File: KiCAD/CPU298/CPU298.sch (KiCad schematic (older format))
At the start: 1 part

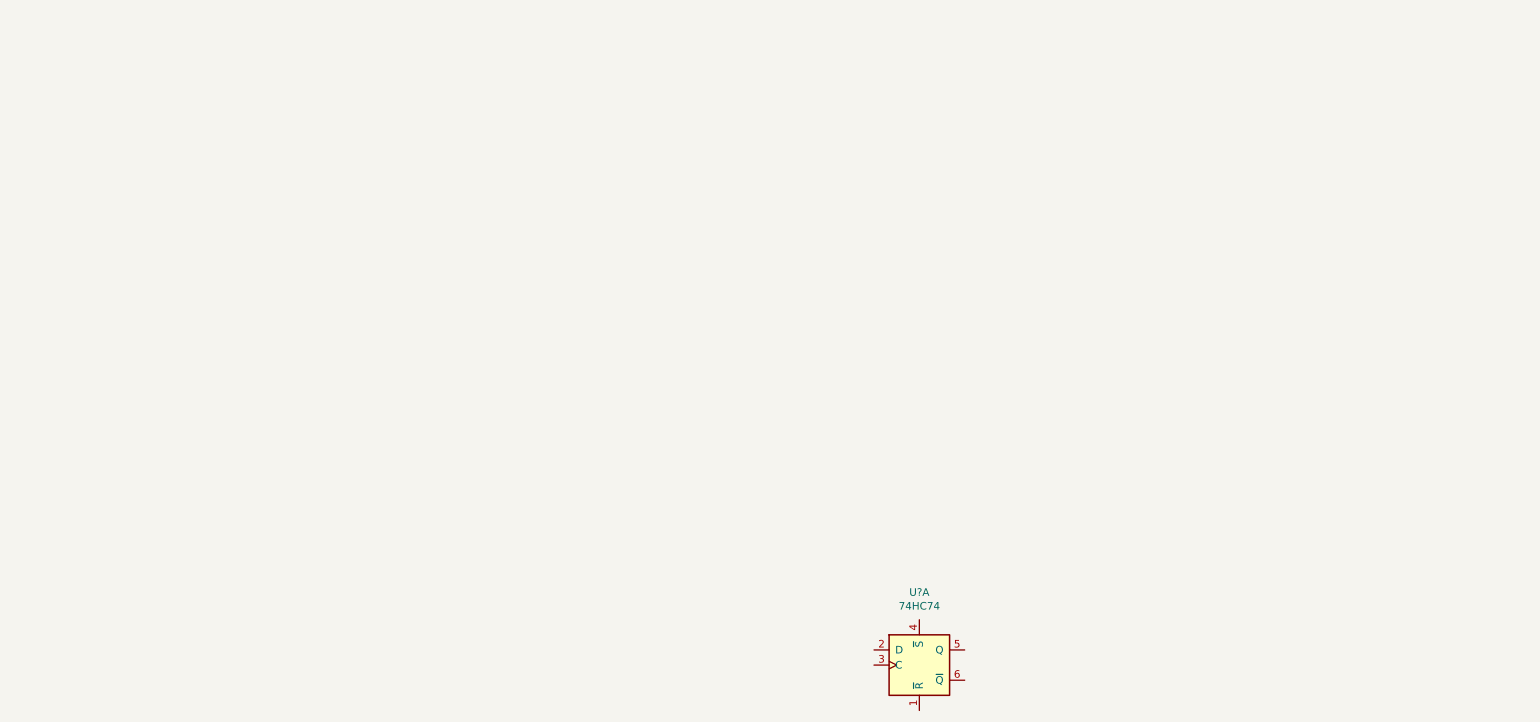
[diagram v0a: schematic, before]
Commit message: 8bit offset adder.
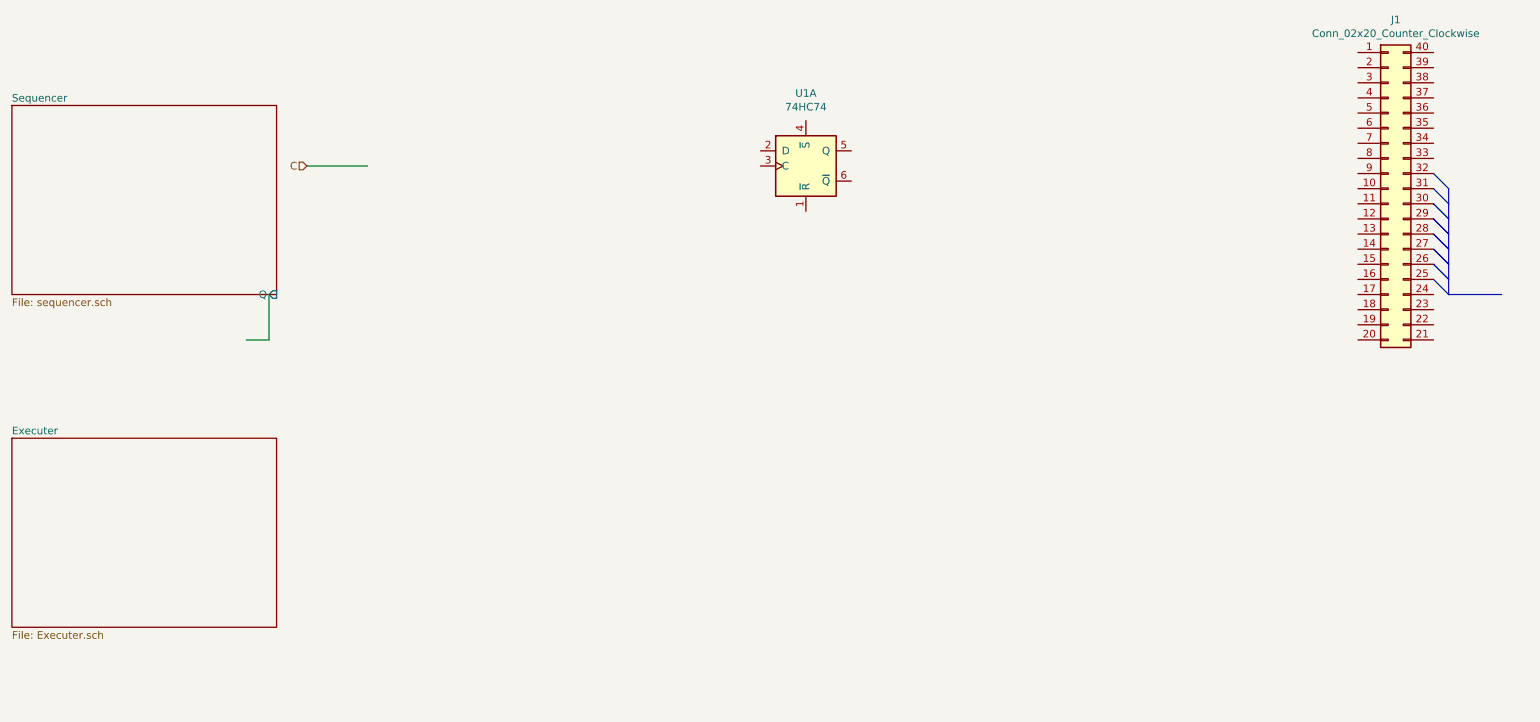
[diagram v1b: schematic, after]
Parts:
- added J1: Conn_02x20_Counter_Clockwise, symbol Connector_Generic:Conn_02x20_Counter_Clockwise
- gave numbers to parts that had none: 1
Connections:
- net labels added: C
- wire segments 0 -> 3
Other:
- moved on the sheet: U1A
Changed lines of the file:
@@
 $Descr A4 11693 8268
 encoding utf-8
-Sheet 1 1
+Sheet 1 3
 Title ""
 Date ""
@@
 $EndDescr
 $Comp
-L 74xx:74HC74 U?
+L 74xx:74HC74 U1
 U 1 1 61108220
-P 7050 5500
-F 0 "U?" H 7050 5981 50  0000 C CNN
-F 1 "74HC74" H 7050 5890 50  0000 C CNN
-F 2 "" H 7050 5500 50  0001 C CNN
-F 3 "74xx/74hc_hct74.pdf" H 7050 5500 50  0001 C CNN
-	1    7050 5500
+P 6300 2200
+F 0 "U1" H 6300 2681 50  0000 C CNN
+F 1 "74HC74" H 6300 2590 50  0000 C CNN
+F 2 "" H 6300 2200 50  0001 C CNN
+F 3 "74xx/74hc_hct74.pdf" H 6300 2200 50  0001 C CNN
+	1    6300 2200
 	1    0    0    -1
 $EndComp
+$Sheet
+S 1050 1800 1750 1250
+U 64746FA5
+F0 "Sequencer" 50
+F1 "sequencer.sch" 50
+F2 "Q" I R 2800 3050 50
+$EndSheet
+$Sheet
+S 1050 4000 1750 1250
+U 6474704B
+F0 "Executer" 50
+F1 "Executer.sch" 50
+$EndSheet
+$Comp
+L Connector_Generic:Conn_02x20_Counter_Clockwise J1
+U 1 1 6474722C
+P 10150 2350
+F 0 "J1" H 10200 3467 50  0000 C CNN
+F 1 "Conn_02x20_Counter_Clockwise" H 10200 3376 50  0000 C CNN
+F 2 "" H 10150 2350 50  0001 C CNN
+F 3 "~" H 10150 2350 50  0001 C CNN
+	1    10150 2350
+	1    0    0    -1
+$EndComp
+Entry Bus Bus
+	10450 2250 10550 2350
+Entry Bus Bus
+	10450 2350 10550 2450
+Entry Bus Bus
+	10450 2450 10550 2550
+Entry Bus Bus
+	10450 2550 10550 2650
+Entry Bus Bus
+	10450 2650 10550 2750
+Entry Bus Bus
+	10450 2750 10550 2850
+Entry Bus Bus
+	10450 2850 10550 2950
+Entry Bus Bus
+	10450 2950 10550 3050
+Wire Bus Line
+	10550 3050 10900 3050
+Text HLabel 3000 2200 0    50   Input ~ 0
+C
+Wire Wire Line
+	3000 2200 3400 2200
+Wire Wire Line
+	2750 3050 2750 3350
+Wire Wire Line
+	2750 3350 2600 3350
+Wire Bus Line
+	10550 2350 10550 3050
 $EndSCHEMATC

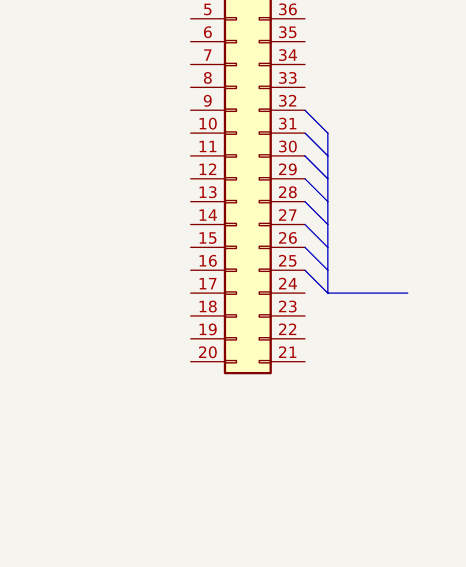
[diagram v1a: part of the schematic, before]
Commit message: Support Int trap
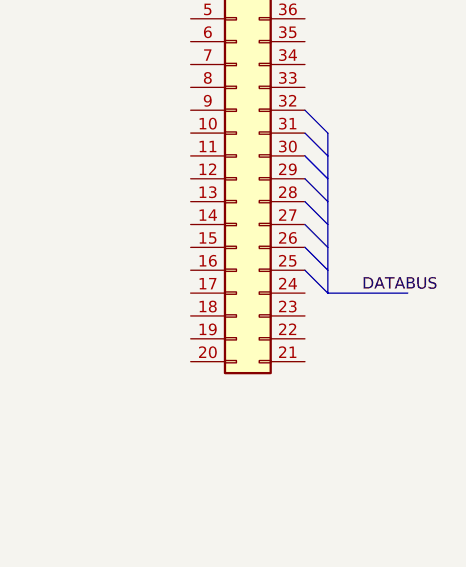
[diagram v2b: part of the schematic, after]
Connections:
- net labels added: DATABUS
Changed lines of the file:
@@
 Wire Bus Line
 	10550 2350 10550 3050
+Text Label 10700 3050 0    50   ~ 0
+DATABUS
 $EndSCHEMATC
